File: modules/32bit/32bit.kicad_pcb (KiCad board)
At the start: 4 copper layers, 30.5 x 68.6 mm, 62 parts, among them J5 USB_C_Receptacle_USB2.0_14P, SW1 K2-1808SN-A4SW-01, SW2 K2-1808SN-A4SW-01, SW4 K2-1808SN-A4SW-01, U1 ESP32-S3-WROOM-1U-N16R8, U3 MCP6002-xSN

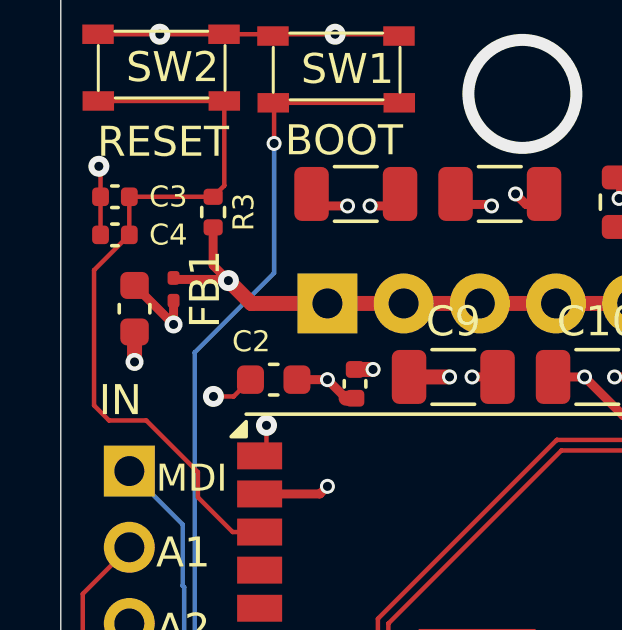
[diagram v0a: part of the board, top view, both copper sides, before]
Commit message: 32bit: Use a known ferrite bead
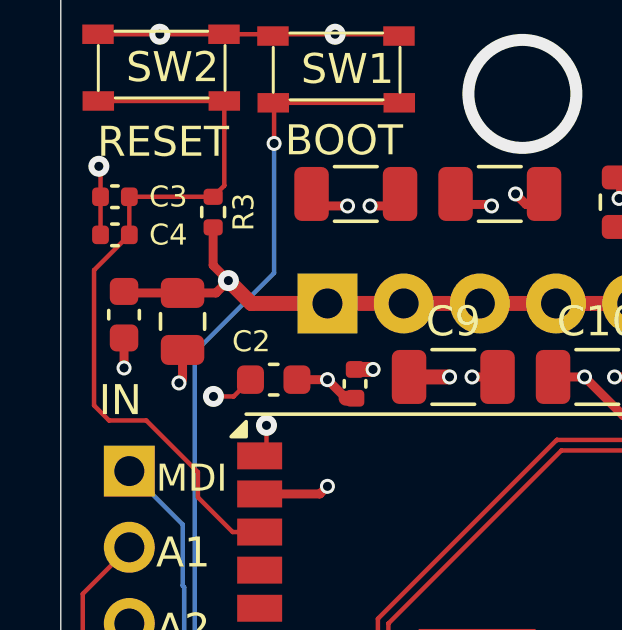
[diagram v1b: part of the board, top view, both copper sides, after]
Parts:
- FB1: value BLM18PG121 -> GZ2012D121TF; footprint Capacitor_SMD:C_0201_0603Metric -> Capacitor_SMD:C_0805_2012Metric
- moved FB1 1.12 mm to (51.0, 51.4), turned to 90 degrees
- moved C8 0.40 mm to (49.1, 51.2)
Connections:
- C8 pad 2: +3V3_ESP32 -> +3V3
- FB1 pad 1: +3V3 -> +3V3_ESP32
- FB1 pad 2: +3V3_ESP32 -> +3V3
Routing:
- net +3V3_ESP32: track 65.1 -> 62.8 mm
- net +3V3: track 89.6 -> 91.5 mm
